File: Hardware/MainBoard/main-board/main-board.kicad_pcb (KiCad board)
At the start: 4 copper layers, 111 parts, among them J1 1366005, J10 4DB-P108-02, J11 Conn_01x04, J12 Conn_01x05, J13 Conn_01x04, J14 Conn_01x06, J15 Conn_01x08, J2 Conn_01x02, J3 Conn_01x02, J4 Conn_01x03, J5 1366005, J6 Conn_01x07, J7 Conn_01x04, J8 Conn_01x02, J9 Conn_01x02, Q1 IRLML6244TRPBF, Q2 IRLML6244TRPBF, Q3 IRLML6244TRPBF, Q4 IRLML6244TRPBF, SW1 SW_SPST, SW2 SW_SPDT, U1 MCP1727T-3302E/SN, U2 DS18B20+, U3 MOC3083S-TA1, U4 STM32F401RETx, U5 OPA333AIDCKT, U6 OPA333AIDCKT, U7 DS18B20+, Y2 ATS08A-E

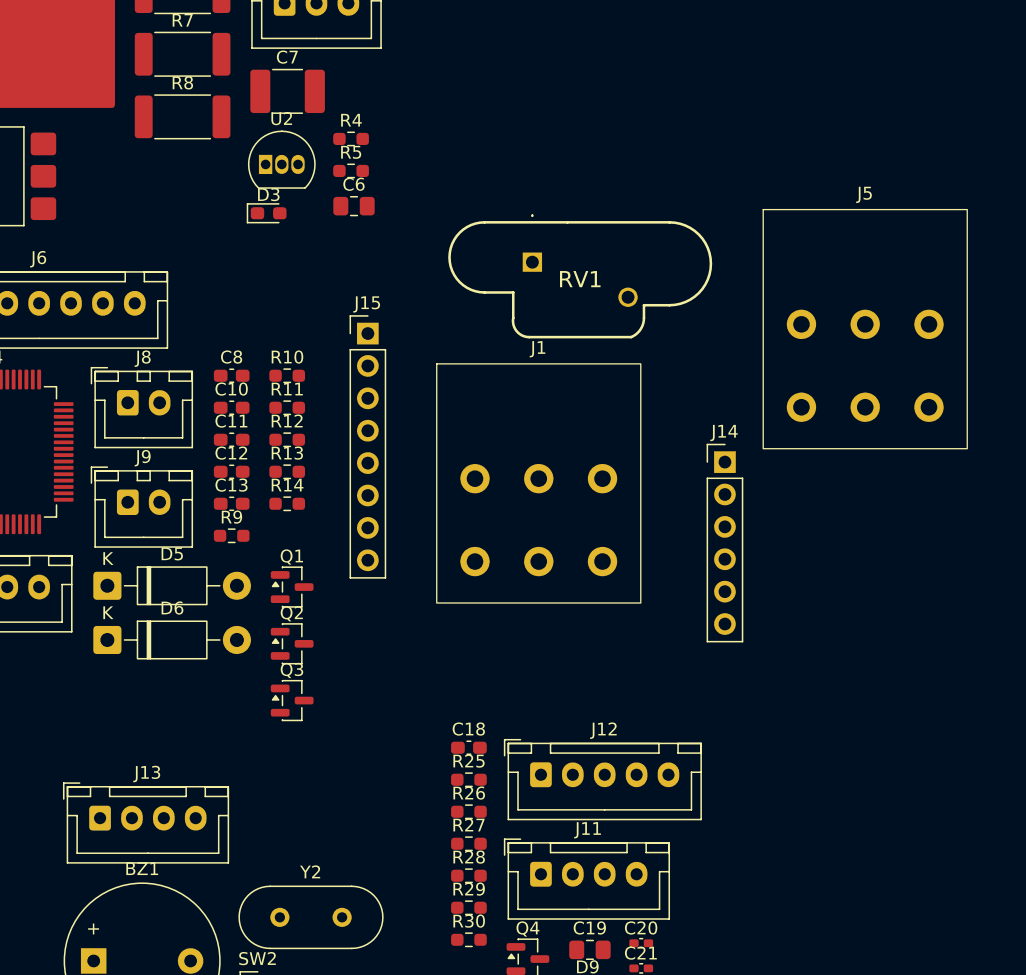
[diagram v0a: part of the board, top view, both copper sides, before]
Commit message: add heatsink mounting holes, change a few footprints, clean up schematic
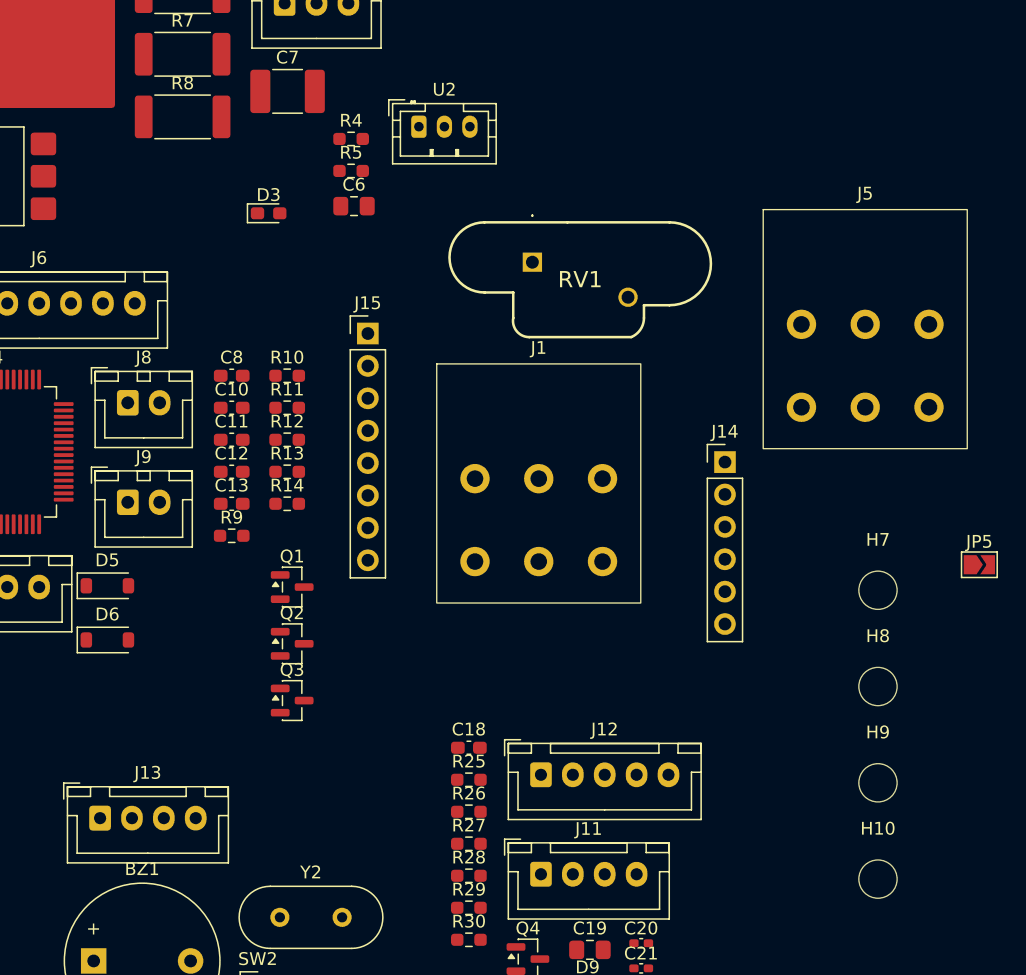
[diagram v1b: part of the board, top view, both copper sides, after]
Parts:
- added H10: MountingHole, MountingHole:MountingHole_3mm, F.Cu at (254.0, 123.0)
- added H7: MountingHole, MountingHole:MountingHole_3mm, F.Cu at (254.0, 100.3)
- added H8: MountingHole, MountingHole:MountingHole_3mm, F.Cu at (254.0, 107.9)
- added H9: MountingHole, MountingHole:MountingHole_3mm, F.Cu at (254.0, 115.5)
- added JP5: Jumper_2_Open, Jumper:SolderJumper-2_P1.3mm_Open_TrianglePad1.0x1.5mm, F.Cu at (261.9, 98.3)
- D5, D6: value 1N5819 -> 1N5819HW-7-F; footprint Diode_THT:D_DO-41_SOD81_P10.16mm_Horizontal -> Diode_SMD:D_SOD-123
- U2: footprint Package_TO_SOT_THT:TO-92_Inline -> Connector_JST:JST_PH_B3B-PH-K_1x03_P2.00mm_Vertical
- moved U2 12.4 mm to (218.0, 64.0)
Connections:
- R24 pad 1: Net-(JP4-B) -> /Block Diagram/Thermocouple Page 6/TC_S2_OUT

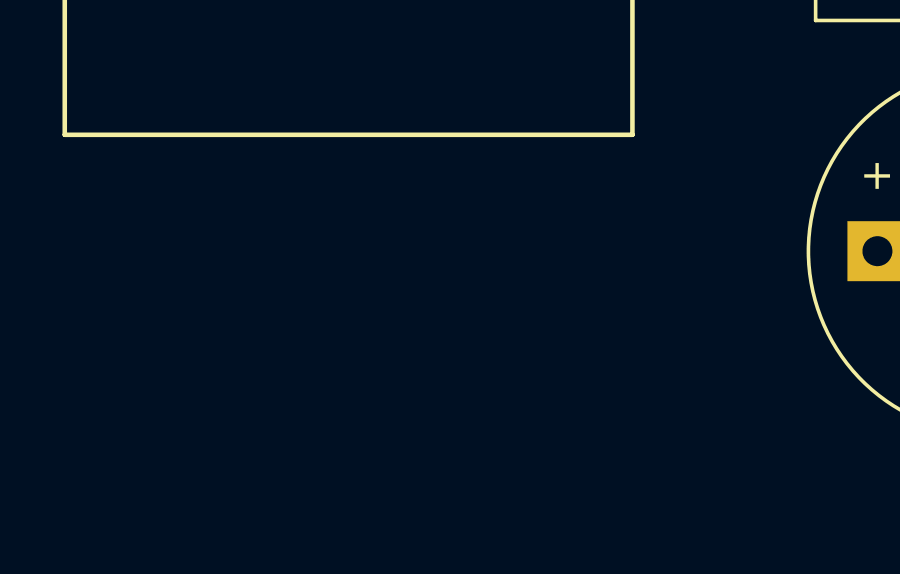
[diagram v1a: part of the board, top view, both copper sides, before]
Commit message: add capacitance to 5v power supply
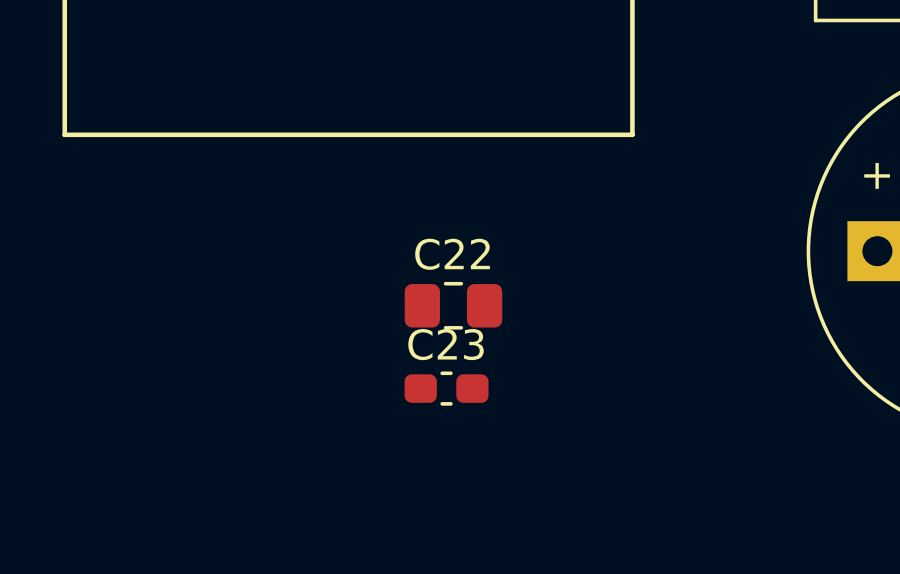
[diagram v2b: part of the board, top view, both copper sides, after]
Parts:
- added C22: 1uF, Capacitor_SMD:C_0805_2012Metric_Pad1.18x1.45mm_HandSolder, F.Cu at (178.4, 131.2)
- added C23: 100nF, Capacitor_SMD:C_0603_1608Metric_Pad1.08x0.95mm_HandSolder, F.Cu at (178.1, 134.0)
- C4: value 100uF -> 47uF

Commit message: working on PCB layout
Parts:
- added D10: 1N5819HW-7-F, Diode_SMD:D_SOD-123, F.Cu at (116.8, 145.7)
- added J16: Conn_01x03, Connector_JST:JST_XH_B3B-XH-A_1x03_P2.50mm_Vertical, F.Cu at (121.0, 140.0)
- added Q5: IRLML6244TRPBF, Package_TO_SOT_SMD:SOT-23, F.Cu at (122.4, 147.1)
- added R31: 1k, Resistor_SMD:R_0603_1608Metric_Pad0.98x0.95mm_HandSolder, F.Cu at (120.0, 151.0)
- added R32: 10k, Resistor_SMD:R_0603_1608Metric_Pad0.98x0.95mm_HandSolder, F.Cu at (123.0, 151.0)
- moved C15 362.5 mm to (514.4, 71.2)
- moved C16 362.5 mm to (514.4, 74.2)
- moved C17 362.5 mm to (514.4, 77.2)
- moved JP5 362.5 mm to (622.6, 61.2)
- moved NT1 362.5 mm to (586.1, 98.2)
- moved BZ1 362.5 mm to (553.1, 92.2)
- moved C10 362.5 mm to (564.0, 48.9)
- moved C11 362.5 mm to (564.0, 51.4)
- moved C12 362.5 mm to (564.0, 53.9)
- moved C13 362.5 mm to (564.0, 56.4)
- moved C14 362.5 mm to (501.4, 70.9)
- moved C18 362.5 mm to (582.6, 75.5)
- moved C19 362.5 mm to (592.0, 91.4)
- moved C20 362.5 mm to (596.1, 90.8)
- moved C21 362.5 mm to (596.1, 92.8)
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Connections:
- U4 pad 59: unconnected-(U4-PB7-Pad59) -> Fan3
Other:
- board outline added: 290 x 85 mm
- board text added: "AC Input"
- board text added: "AC Output"
- board text added: "COLD"
- board text added: "Front"
- board text added: "HOT"

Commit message: routing halfway done, trying autorouter to finish low voltage signals
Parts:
- removed JP4: Jumper_2_Open, Connector_PinHeader_2.54mm:PinHeader_1x02_P2.54mm_Vertical
- added G***: LOGO, LOGO, F.Cu at (201.8, 136.5)
- added G***: LOGO, LOGO, F.Cu at (74.8, 123.2)
- added REF**: MTP Logo 5mm Low Detail, Watermarks:MTP Logo 5mm Low Detail, F.Cu at (393.8, 157.5)
- added REF**: MTP Logo 5mm Low Detail Copper, Watermarks:MTP Logo 5mm Low Detail Copper, F.Cu at (292.5, 161.0)
- added REF**: MTP Logo 10mm Low Detail, Watermarks:MTP Logo 10mm Low Detail, F.Cu at (202.5, 118.5)
- moved J14 493.2 mm to (120.2, 155.8)
- moved R5 457.8 mm to (131.8, 151.0), turned to 90 degrees
- moved R4 457.0 mm to (136.0, 160.5), turned to -90 degrees
- moved D3 448.1 mm to (136.0, 156.8), turned to 90 degrees
- moved R10 440.6 mm to (143.0, 161.5), turned to 90 degrees
- moved Q1 440.2 mm to (139.7, 161.5), turned to 180 degrees
- moved R9 435.2 mm to (141.8, 164.5), turned to 180 degrees
- moved D9 433.4 mm to (163.8, 162.0)
- moved R27 430.1 mm to (159.8, 162.0), turned to 180 degrees
- moved J4 429.3 mm to (129.7, 162.8), turned to 90 degrees
- moved R11 427.7 mm to (157.0, 166.0), turned to 180 degrees
- moved Q2 427.5 mm to (153.0, 166.9), turned to 90 degrees
- moved R13 426.8 mm to (157.0, 168.0)
- moved C20 424.9 mm to (176.2, 156.5), turned to -90 degrees
- moved C21 424.3 mm to (176.2, 154.1), turned to 90 degrees
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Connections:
- D10 pad 2: /Block Diagram/MCU Page 5/FAN2_MINUS -> /Block Diagram/MCU Page 5/FAN3_MINUS
- J16 pad 2: /Block Diagram/MCU Page 5/FAN2_MINUS -> /Block Diagram/MCU Page 5/FAN3_MINUS
- Q5 pad 1: /Block Diagram/MCU Page 5/FAN2_FET_G -> /Block Diagram/MCU Page 5/FAN3_FET_G
- Q5 pad 3: /Block Diagram/MCU Page 5/FAN2_MINUS -> /Block Diagram/MCU Page 5/FAN3_MINUS
- R16 pad 1: /Block Diagram/Thermocouple Page 6/TC_S1_- -> /Block Diagram/Thermocouple Page 6/TC_S2_PD
- R16 pad 2: /Block Diagram/Thermocouple Page 6/TC_S1_PD -> GND
- R17 pad 1: /Block Diagram/Thermocouple Page 6/TC_S1_PD -> /Block Diagram/Thermocouple Page 6/TC_S2_-
- R17 pad 2: GND -> /Block Diagram/Thermocouple Page 6/TC_S2_PD
- R18 pad 1: /Block Diagram/Thermocouple Page 6/TC_S1_- -> /Block Diagram/Thermocouple Page 6/TC_S2_-
- R18 pad 2: /Block Diagram/Thermocouple Page 6/TC_S1_FB -> /Block Diagram/Thermocouple Page 6/TC_S2_FB
- R19 pad 2: /Block Diagram/Thermocouple Page 6/TC_S1_FB -> /Block Diagram/Thermocouple Page 6/TC_S2_FB
- R20 pad 1: /Block Diagram/Thermocouple Page 6/TC_S1_- -> /Block Diagram/Thermocouple Page 6/TC_S2_PD
- R20 pad 2: /Block Diagram/Thermocouple Page 6/TC_S2_PD -> GND
- R21 pad 1: /Block Diagram/Thermocouple Page 6/TC_S2_PD -> /Block Diagram/Thermocouple Page 6/TC_S1_-
- R21 pad 2: GND -> /Block Diagram/Thermocouple Page 6/TC_S2_PD
- R31 pad 2: /Block Diagram/MCU Page 5/FAN2_FET_G -> /Block Diagram/MCU Page 5/FAN3_FET_G
- R32 pad 1: /Block Diagram/MCU Page 5/FAN2_FET_G -> /Block Diagram/MCU Page 5/FAN3_FET_G
- U4 pad 1: +3.3VA -> +3.3V
- U5 pad 4: /Block Diagram/Thermocouple Page 6/TC_S1_- -> /Block Diagram/Thermocouple Page 6/TC_S2_-
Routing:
- net +3.3V: track 0.00 -> 410.0 mm, vias 0 -> 2
- net +5V: track 0.00 -> 391.8 mm, vias 0 -> 3
- net +3.3VA: track 0.00 -> 173.8 mm, vias 0 -> 10
- net TC_JCT_TEMP: track 0.00 -> 146.7 mm, vias 0 -> 3
- net KP_Row3: track 0.00 -> 118.1 mm, vias 0 -> 1
- net KP_Row2: track 0.00 -> 115.8 mm, vias 0 -> 1
- net KP_Row1: track 0.00 -> 113.2 mm, vias 0 -> 1
- net KP_Row0: track 0.00 -> 109.9 mm, vias 0 -> 1
- net GND: track 0.00 -> 104.8 mm, vias 0 -> 32
- net PC11: track 0.00 -> 75.6 mm, vias 0 -> 3
- net PC10: track 0.00 -> 74.2 mm, vias 0 -> 3
- net PD2: track 0.00 -> 73.6 mm, vias 0 -> 1
- net Fan3: track 0.00 -> 71.7 mm, vias 0 -> 2
- net /Block Diagram/MCU Page 5/HEAT_OUT: track 0.00 -> 57.9 mm, vias 0 -> 4
- net Fan1: track 0.00 -> 46.8 mm, vias 0 -> 4
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- added copper zone on In1.Cu, net GND
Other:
- board size 290 x 85 mm -> 229.8 x 85 mm
- board text added: "+ -"
- board text added: "+3V3"
- board text added: "+3v3"
- board text added: "+5V"
- board text added: "+5v"
- board text added: "1A Fuse"
- board text added: "20A Fuse"
- board text added: "3V3 +"
- board text added: "3V3 Enable"
- board text added: "5V +"
- board text added: "5V Enable"
- board text added: "AC Power Switch for 5V PSU"
- board text added: "Boot0"
- board text added: "CAUTION 120VAC"
- board text added: "Caution! Mains Voltage"
- board text added: "DS18B20"
- board text added: "Des. by Michael Pate v2.0 02/2026"
- board text added: "Fan 1"
- board text added: "Fan 2"
- board text added: "GND"
- board text added: "Heatsink Fan"
- board text added: "Heatsink Temp. Sensor"
- board text added: "High Voltage! Disconnect AC before programming."
- board text added: "Input Power"
- board text added: "Keypad"
- board text added: "L GND N"
- board text added: "OLED"
- board text added: "Output Power"
- board text added: "PB0"
- board text added: "PB1"
- board text added: "PB2"
- board text added: "PC10"
- board text added: "PC11"
- board text added: "PC8"
- board text added: "PC9"
- board text added: "PD2"
- board text added: "PROTOTYPE"
- board text added: "Power/Reset"
- board text added: "STLINK"
- board text added: "Sig"
- board text added: "Spare IO"
- board text added: "Stage 2 Enable"
- board text added: "TC Enable"
- board text added: "TRIAC"
- board text added: "Thermocouple"
- board text added: "Toaster-Flo 2000"
- board text added: "USER"

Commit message: Finish board layout
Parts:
- removed the REF** at (393.8, 157.5)
- moved C7 2.00 mm to (163.0, 103.0)
- moved R7 2.00 mm to (142.0, 118.0)
- moved R8 2.00 mm to (176.0, 103.0)
- moved F1 1.00 mm to (117.2, 95.0)
- moved R6 0.50 mm to (140.5, 131.0)
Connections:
- J1 pad 1: LN -> L1
- J1 pad 3: L1 -> LN
- J15 pad 1: PB0 -> PC9
- J15 pad 2: PB1 -> PC8
- J15 pad 3: PB2 -> PB0
- J15 pad 4: PC8 -> PB1
- J15 pad 5: PC9 -> PB2
- J5 pad 1: L1 -> /Block Diagram/TRIAC Page 4/L1_HEATER
- J5 pad 3: /Block Diagram/TRIAC Page 4/L1_HEATER -> L1
- J6 pad 1: KP_Col2 -> KP_Col0
- J6 pad 3: KP_Col0 -> KP_Col2
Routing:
- net KP_Col2: track 0.00 -> 138.0 mm, vias 0 -> 4
- net KP_Col1: track 0.00 -> 128.8 mm, vias 0 -> 2
- net KP_Col0: track 0.00 -> 125.3 mm, vias 0 -> 2
- net SPI_MISO: track 0.00 -> 122.1 mm, vias 0 -> 3
- net SPI_CLK: track 0.00 -> 116.9 mm, vias 0 -> 6
- net TC_CS: track 0.00 -> 107.9 mm, vias 0 -> 1
- net Soft_Power: track 0.00 -> 106.6 mm, vias 0 -> 2
- net TC_VOUT: track 3.05 -> 107.8 mm, vias 0 -> 2
- net NRST_SW: track 7.39 -> 110.6 mm, vias 0 -> 2
- net Fan2: track 0.00 -> 88.6 mm, vias 0 -> 4
- net I2C_CLK: track 0.00 -> 86.3 mm, vias 0 -> 1
- net PB0: track 0.00 -> 84.7 mm, vias 0 -> 1
- net I2C_SDA: track 0.00 -> 84.2 mm, vias 0 -> 2
- net PC9: track 0.00 -> 82.1 mm, vias 0 -> 1
- net PB1: track 0.00 -> 80.8 mm, vias 0 -> 1
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- added copper zone on F.Cu, net /Block Diagram/TRIAC Page 4/L1_F2
- added copper zone on F.Cu, net /Block Diagram/TRIAC Page 4/L1_F2_RC
- added copper zone on F.Cu, net /Block Diagram/TRIAC Page 4/L1_HEATER
- added copper zone on In2.Cu, net GND
- added copper zone on B.Cu, net GNDPWR
- added copper zone on F.Cu, net L1
- added copper zone on F.Cu, net LN
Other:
- board text added: "+"
- board text added: "+ D -"
- board text added: "+3.3v"
- board text added: "CS"
- board text added: "Clock"
- board text added: "Col 0"
- board text added: "Col 1"
- board text added: "Col 2"
- board text added: "MAX6675"
- board text added: "MISO"
- board text added: "N GND L"
- board text added: "Power"
- board text added: "Reset"
- board text added: "Row 0"
- board text added: "Row 1"
- board text added: "Row 2"
- board text added: "Row 3"
- board text added: "SCL"
- board text added: "SDA"
- board text added: "SWDCLK"
- board text added: "SWDIO"
- board text added: "Tie Boot0 to GND for normal operation"
- board text removed: "L GND N"
